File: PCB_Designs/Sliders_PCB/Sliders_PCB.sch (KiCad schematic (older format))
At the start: 7 parts, among them P1 CONN_01X06

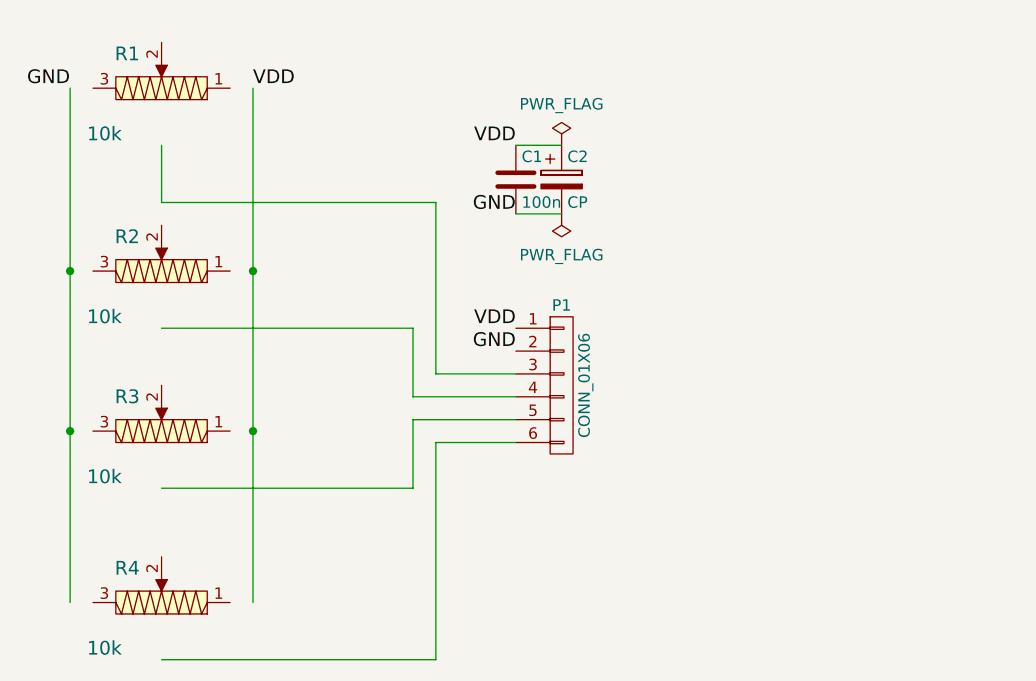
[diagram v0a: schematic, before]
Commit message: PTA6043, Sliders_PCB
Added:
PTA 6043 .lib and .pretty

Drew traces to Sliders_PCB (v1)
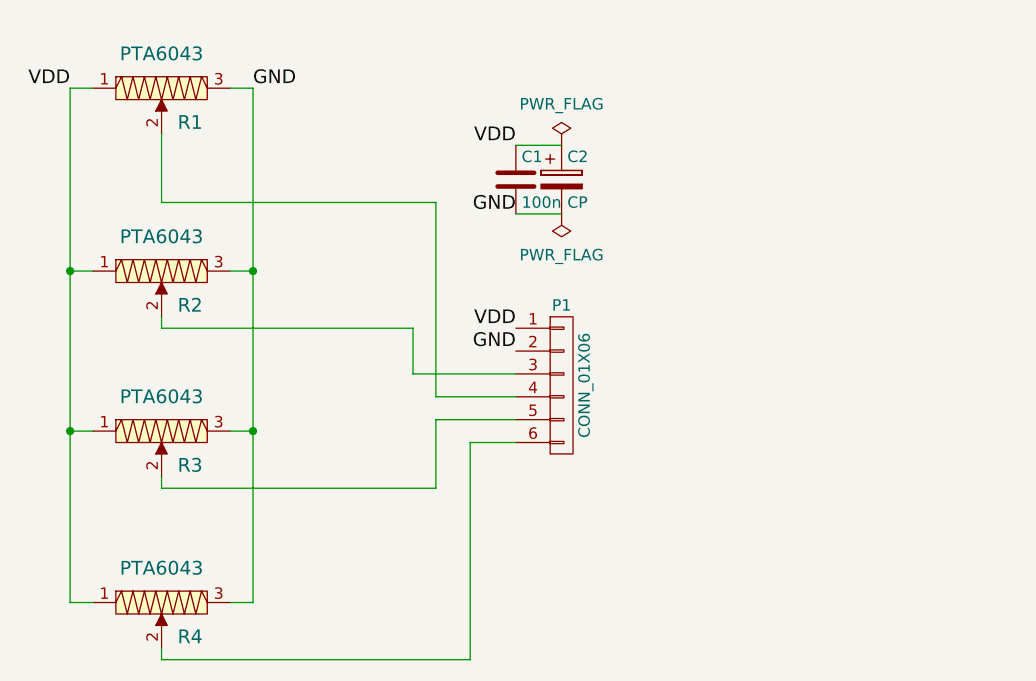
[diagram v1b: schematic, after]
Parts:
- R1, R2, R3, R4: value 10k -> PTA6043; footprint PTA6043:PTA6043 -> Potentiometers_Bourne:Potentiometer_Bourns-PTA6043
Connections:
- wire segments 17 -> 28
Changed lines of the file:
@@
 EESchema Schematic File Version 2
-LIBS:PTA6043
+LIBS:Custom_Switches
 LIBS:mcdts2-4n
-LIBS:conn_01x06_Buttons
 LIBS:power
 LIBS:device
@@
 LIBS:contrib
 LIBS:valves
+LIBS:Slide_Potentiometer
 LIBS:Sliders_PCB-cache
 EELAYER 25 0
@@
 $EndDescr
 $Comp
-L PTA6043 R4
-U 1 1 588B4999
-P 4650 3250
-F 0 "R4" H 4800 3100 60  0000 C CNN
-F 1 "10k" H 4900 3450 60  0000 C CNN
-F 2 "PTA6043:PTA6043" H 4650 3250 60  0001 C CNN
-F 3 "" H 4650 3250 60  0001 C CNN
-	1    4650 3250
-	-1   0    0    1
-$EndComp
-$Comp
-L PTA6043 R3
-U 1 1 588B4A8C
-P 4650 2500
-F 0 "R3" H 4800 2350 60  0000 C CNN
-F 1 "10k" H 4900 2700 60  0000 C CNN
-F 2 "PTA6043:PTA6043" H 4650 2500 60  0001 C CNN
-F 3 "" H 4650 2500 60  0001 C CNN
-	1    4650 2500
-	-1   0    0    1
-$EndComp
-$Comp
-L PTA6043 R2
-U 1 1 588B4AAC
-P 4650 1800
-F 0 "R2" H 4800 1650 60  0000 C CNN
-F 1 "10k" H 4900 2000 60  0000 C CNN
-F 2 "PTA6043:PTA6043" H 4650 1800 60  0001 C CNN
-F 3 "" H 4650 1800 60  0001 C CNN
-	1    4650 1800
-	-1   0    0    1
-$EndComp
-$Comp
-L PTA6043 R1
-U 1 1 588B4B8B
-P 4650 1000
-F 0 "R1" H 4800 850 60  0000 C CNN
-F 1 "10k" H 4900 1200 60  0000 C CNN
-F 2 "PTA6043:PTA6043" H 4650 1000 60  0001 C CNN
-F 3 "" H 4650 1000 60  0001 C CNN
-	1    4650 1000
-	-1   0    0    1
-$EndComp
-$Comp
 L CONN_01X06 P1
 U 1 1 588B4D25
@@
 	1    0    0    -1
 $EndComp
+Text Label 4250 1000 2    60   ~ 0
+VDD
 Text Label 5050 1000 0    60   ~ 0
-VDD
-Text Label 4250 1000 2    60   ~ 0
 GND
 Wire Wire Line
@@
 Connection ~ 4250 2500
 Wire Wire Line
-	4650 1250 4650 1500
+	4650 1200 4650 1500
 Wire Wire Line
 	4650 1500 5850 1500
 Wire Wire Line
-	5850 1500 5850 2250
-Wire Wire Line
-	5850 2250 6200 2250
-Wire Wire Line
-	6200 2350 5750 2350
-Wire Wire Line
-	5750 2350 5750 2050
+	5850 1500 5850 2350
 Wire Wire Line
 	5750 2050 4650 2050
 Wire Wire Line
-	4650 2750 5750 2750
-Wire Wire Line
-	5750 2750 5750 2450
-Wire Wire Line
-	5750 2450 6200 2450
-Wire Wire Line
-	6200 2550 5850 2550
-Wire Wire Line
-	5850 2550 5850 3500
-Wire Wire Line
-	5850 3500 4650 3500
+	4650 3500 6000 3500
 $Comp
 L PWR_FLAG #GND02
@@
 	1    0    0    -1
 $EndComp
+$Comp
+L PTA6043 R1
+U 1 1 589238E9
+P 4650 1000
+F 0 "R1" H 4775 850 60  0000 C CNN
+F 1 "PTA6043" H 4650 1150 60  0000 C CNN
+F 2 "Potentiometers_Bourne:Potentiometer_Bourns-PTA6043" H 4600 1375 60  0001 C CNN
+F 3 "" H 4600 1375 60  0001 C CNN
+	1    4650 1000
+	1    0    0    -1
+$EndComp
+Wire Wire Line
+	4250 1000 4350 1000
+Wire Wire Line
+	4950 1000 5050 1000
+$Comp
+L PTA6043 R2
+U 1 1 589239B0
+P 4650 1800
+F 0 "R2" H 4775 1650 60  0000 C CNN
+F 1 "PTA6043" H 4650 1950 60  0000 C CNN
+F 2 "Potentiometers_Bourne:Potentiometer_Bourns-PTA6043" H 4600 2175 60  0001 C CNN
+F 3 "" H 4600 2175 60  0001 C CNN
+	1    4650 1800
+	1    0    0    -1
+$EndComp
+$Comp
+L PTA6043 R4
+U 1 1 589239FB
+P 4650 3250
+F 0 "R4" H 4775 3100 60  0000 C CNN
+F 1 "PTA6043" H 4650 3400 60  0000 C CNN
+F 2 "Potentiometers_Bourne:Potentiometer_Bourns-PTA6043" H 4600 3625 60  0001 C CNN
+F 3 "" H 4600 3625 60  0001 C CNN
+	1    4650 3250
+	1    0    0    -1
+$EndComp
+$Comp
+L PTA6043 R3
+U 1 1 58923A9D
+P 4650 2500
+F 0 "R3" H 4775 2350 60  0000 C CNN
+F 1 "PTA6043" H 4650 2650 60  0000 C CNN
+F 2 "Potentiometers_Bourne:Potentiometer_Bourns-PTA6043" H 4600 2875 60  0001 C CNN
+F 3 "" H 4600 2875 60  0001 C CNN
+	1    4650 2500
+	1    0    0    -1
+$EndComp
+Wire Wire Line
+	4250 1800 4350 1800
+Wire Wire Line
+	4650 2050 4650 2000
+Wire Wire Line
+	4950 1800 5050 1800
+Wire Wire Line
+	4650 2700 4650 2750
+Wire Wire Line
+	4250 2500 4350 2500
+Wire Wire Line
+	4950 2500 5050 2500
+Wire Wire Line
+	4250 3250 4350 3250
+Wire Wire Line
+	4650 3500 4650 3450
+Wire Wire Line
+	5050 3250 4950 3250
+Wire Wire Line
+	5850 2350 6200 2350
+Wire Wire Line
+	5750 2050 5750 2250
+Wire Wire Line
+	5750 2250 6200 2250
+Wire Wire Line
+	4650 2750 5850 2750
+Wire Wire Line
+	5850 2750 5850 2450
+Wire Wire Line
+	5850 2450 6200 2450
+Wire Wire Line
+	6000 3500 6000 2550
+Wire Wire Line
+	6000 2550 6200 2550
 $EndSCHEMATC

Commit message: Sliders v2
Sliders_PCB klara
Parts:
- removed C2: CP, Capacitors_SMD:CP_Elec_4x4.5, symbol CP
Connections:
- net at P1.3 (P3): now also R1.2; no longer R2.2
- net at P1.4 (P4): now also R2.2; no longer R1.2
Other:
- moved on the sheet: C1
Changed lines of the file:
@@
 Text Label 6200 2150 2    60   ~ 0
 GND
-Text Label 6200 1250 2    60   ~ 0
+Text Label 6450 1250 2    60   ~ 0
 VDD
 $Comp
 L C C1
 U 1 1 588B503E
-P 6200 1400
-F 0 "C1" H 6225 1500 50  0000 L CNN
-F 1 "100n" H 6225 1300 50  0000 L CNN
-F 2 "Capacitors_SMD:C_0603_HandSoldering" H 6238 1250 50  0001 C CNN
-F 3 "" H 6200 1400 50  0000 C CNN
-	1    6200 1400
+P 6650 1400
+F 0 "C1" H 6675 1500 50  0000 L CNN
+F 1 "100n" H 6675 1300 50  0000 L CNN
+F 2 "Capacitors_SMD:C_0603_HandSoldering" H 6688 1250 50  0001 C CNN
+F 3 "" H 6650 1400 50  0000 C CNN
+	1    6650 1400
 	1    0    0    -1
 $EndComp
-Text Label 6200 1550 2    60   ~ 0
+Text Label 6450 1550 2    60   ~ 0
 GND
 $Comp
 L PWR_FLAG #VDD01
 U 1 1 588B50BE
-P 6400 1250
-F 0 "#VDD01" H 6400 1345 50  0001 C CNN
-F 1 "PWR_FLAG" H 6400 1430 50  0000 C CNN
-F 2 "" H 6400 1250 50  0000 C CNN
-F 3 "" H 6400 1250 50  0000 C CNN
-	1    6400 1250
+P 6650 1250
+F 0 "#VDD01" H 6650 1345 50  0001 C CNN
+F 1 "PWR_FLAG" H 6650 1430 50  0000 C CNN
+F 2 "" H 6650 1250 50  0000 C CNN
+F 3 "" H 6650 1250 50  0000 C CNN
+	1    6650 1250
 	1    0    0    -1
 $EndComp
@@
 GND
 Wire Wire Line
-	6200 1550 6400 1550
+	6450 1550 6650 1550
 Wire Wire Line
-	6400 1250 6200 1250
+	6650 1250 6450 1250
 Wire Wire Line
 	5050 1000 5050 3250
@@
 	4650 1200 4650 1500
 Wire Wire Line
-	4650 1500 5850 1500
+	4650 1500 6000 1500
 Wire Wire Line
-	5850 1500 5850 2350
+	6000 1500 6000 2250
 Wire Wire Line
-	5750 2050 4650 2050
+	5850 2050 4650 2050
 Wire Wire Line
 	4650 3500 6000 3500
@@
 L PWR_FLAG #GND02
 U 1 1 588B6CB3
-P 6400 1550
-F 0 "#GND02" H 6400 1645 50  0001 C CNN
-F 1 "PWR_FLAG" H 6400 1730 50  0000 C CNN
-F 2 "" H 6400 1550 50  0000 C CNN
-F 3 "" H 6400 1550 50  0000 C CNN
-	1    6400 1550
+P 6650 1550
+F 0 "#GND02" H 6650 1645 50  0001 C CNN
+F 1 "PWR_FLAG" H 6650 1730 50  0000 C CNN
+F 2 "" H 6650 1550 50  0000 C CNN
+F 3 "" H 6650 1550 50  0000 C CNN
+	1    6650 1550
 	-1   0    0    1
-$EndComp
-$Comp
-L CP C2
-U 1 1 588B6F6B
-P 6400 1400
-F 0 "C2" H 6425 1500 50  0000 L CNN
-F 1 "CP" H 6425 1300 50  0000 L CNN
-F 2 "Capacitors_SMD:CP_Elec_4x4.5" H 6438 1250 50  0001 C CNN
-F 3 "" H 6400 1400 50  0000 C CNN
-	1    6400 1400
-	1    0    0    -1
 $EndComp
 $Comp
@@
 	5050 3250 4950 3250
 Wire Wire Line
-	5850 2350 6200 2350
-Wire Wire Line
-	5750 2050 5750 2250
-Wire Wire Line
-	5750 2250 6200 2250
+	5850 2050 5850 2350
 Wire Wire Line
 	4650 2750 5850 2750
@@
 Wire Wire Line
 	6000 2550 6200 2550
+Wire Wire Line
+	6000 2250 6200 2250
+Wire Wire Line
+	5850 2350 6200 2350
 $EndSCHEMATC

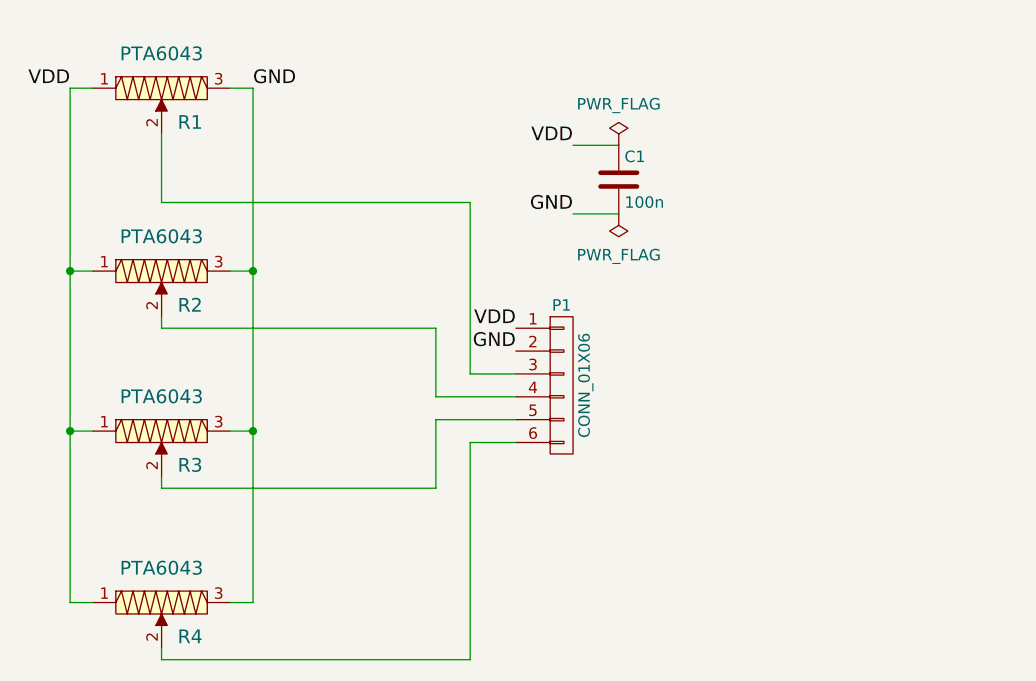
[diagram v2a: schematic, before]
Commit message: Completed all Circuits for evaluation
* All board-to-board connectors now Multicomp 02X05
* Mounting holes for all PCB
* Vias at all groundpins
* Minor other changes
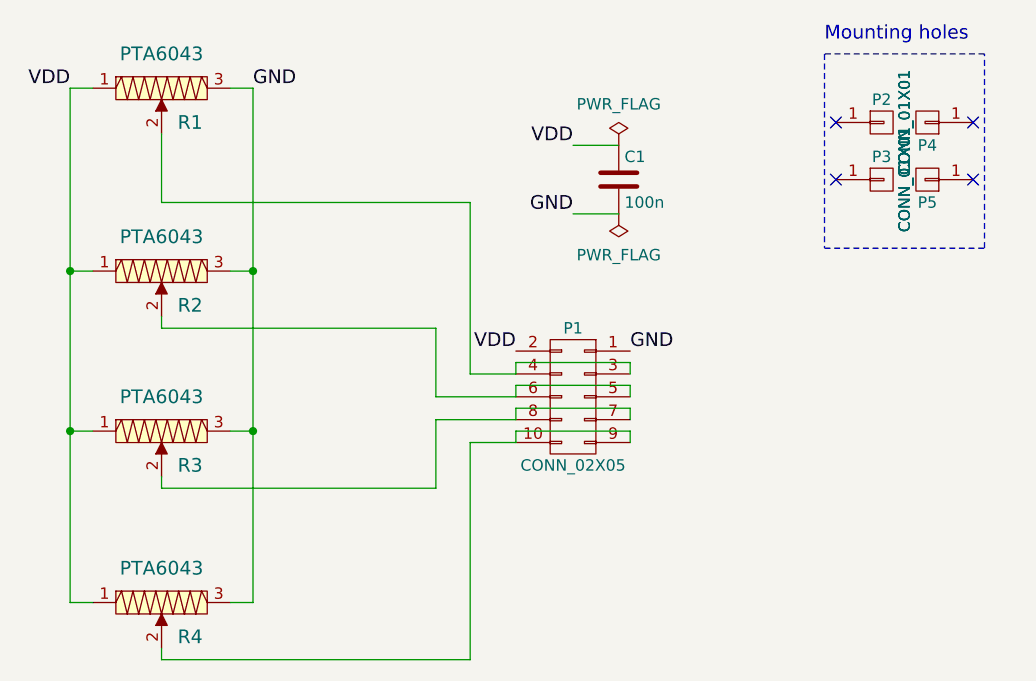
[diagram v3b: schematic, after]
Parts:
- removed P1: CONN_01X06, Socket_Strips:Socket_Strip_Straight_1x06, symbol CONN_01X06
- added P1: CONN_02X05, Connectors_Multicomp:Multicomp_MC9A22-1034_2x05x2.54mm_Angled, symbol CONN_02X05
- added P2, P3, P4, P5: CONN_01X01, Mounting_Holes:MountingHole_2.2mm_M2_DIN965_Pad, symbol CONN_01X01
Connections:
- net GND: now also P1.1 (P1)
- net VDD: now also P1.2 (P2)
- net at R1.2: now also P1.3 (P3), P1.4 (P4)
- net at R2.2: now also P1.5 (P5), P1.6 (P6)
- net at R3.2: now also P1.7 (P7), P1.8 (P8)
- net at R4.2: now also P1.10 (P10), P1.9 (P9)
- no-connect marks 0 -> 4
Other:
- note added: "Mounting holes"
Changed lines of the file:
@@
 Comment4 ""
 $EndDescr
-$Comp
-L CONN_01X06 P1
-U 1 1 588B4D25
-P 6400 2300
-F 0 "P1" H 6400 2650 50  0000 C CNN
-F 1 "CONN_01X06" V 6500 2300 50  0000 C CNN
-F 2 "Socket_Strips:Socket_Strip_Straight_1x06" H 6400 2300 50  0001 C CNN
-F 3 "" H 6400 2300 50  0000 C CNN
-	1    6400 2300
-	1    0    0    -1
-$EndComp
-Text Label 6200 2050 2    60   ~ 0
+Text Label 6200 2150 2    60   ~ 0
 VDD
-Text Label 6200 2150 2    60   ~ 0
+Text Label 6700 2150 0    60   ~ 0
 GND
 Text Label 6450 1250 2    60   ~ 0
@@
 Wire Wire Line
 	5850 2350 6200 2350
+$Comp
+L CONN_02X05 P1
+U 1 1 58A664D3
+P 6450 2350
+F 0 "P1" H 6450 2650 50  0000 C CNN
+F 1 "CONN_02X05" H 6450 2050 50  0000 C CNN
+F 2 "Connectors_Multicomp:Multicomp_MC9A22-1034_2x05x2.54mm_Angled" H 6450 1150 50  0001 C CNN
+F 3 "" H 6450 1150 50  0001 C CNN
+	1    6450 2350
+	-1   0    0    -1
+$EndComp
+Wire Wire Line
+	6200 2250 6200 2200
+Wire Wire Line
+	6200 2200 6700 2200
+Wire Wire Line
+	6700 2200 6700 2250
+Wire Wire Line
+	6200 2350 6200 2300
+Wire Wire Line
+	6200 2300 6700 2300
+Wire Wire Line
+	6700 2300 6700 2350
+Wire Wire Line
+	6700 2450 6700 2400
+Wire Wire Line
+	6700 2400 6200 2400
+Wire Wire Line
+	6200 2400 6200 2450
+Wire Wire Line
+	6200 2550 6200 2500
+Wire Wire Line
+	6200 2500 6700 2500
+Wire Wire Line
+	6700 2500 6700 2550
+$Comp
+L CONN_01X01 P2
+U 1 1 58A619C7
+P 7800 1150
+F 0 "P2" H 7800 1250 50  0000 C CNN
+F 1 "CONN_01X01" V 7900 1150 50  0000 C CNN
+F 2 "Mounting_Holes:MountingHole_2.2mm_M2_DIN965_Pad" H 7800 1150 50  0001 C CNN
+F 3 "" H 7800 1150 50  0001 C CNN
+	1    7800 1150
+	1    0    0    -1
+$EndComp
+$Comp
+L CONN_01X01 P3
+U 1 1 58A61A91
+P 7800 1400
+F 0 "P3" H 7800 1500 50  0000 C CNN
+F 1 "CONN_01X01" V 7900 1400 50  0000 C CNN
+F 2 "Mounting_Holes:MountingHole_2.2mm_M2_DIN965_Pad" H 7800 1400 50  0001 C CNN
+F 3 "" H 7800 1400 50  0001 C CNN
+	1    7800 1400
+	1    0    0    -1
+$EndComp
+$Comp
+L CONN_01X01 P4
+U 1 1 58A61AF0
+P 8000 1150
+F 0 "P4" H 8000 1250 50  0000 C CNN
+F 1 "CONN_01X01" V 8100 1150 50  0000 C CNN
+F 2 "Mounting_Holes:MountingHole_2.2mm_M2_DIN965_Pad" H 8000 1150 50  0001 C CNN
+F 3 "" H 8000 1150 50  0001 C CNN
+	1    8000 1150
+	-1   0    0    1
+$EndComp
+$Comp
+L CONN_01X01 P5
+U 1 1 58A61B35
+P 8000 1400
+F 0 "P5" H 8000 1500 50  0000 C CNN
+F 1 "CONN_01X01" V 8100 1400 50  0000 C CNN
+F 2 "Mounting_Holes:MountingHole_2.2mm_M2_DIN965_Pad" H 8000 1400 50  0001 C CNN
+F 3 "" H 8000 1400 50  0001 C CNN
+	1    8000 1400
+	-1   0    0    1
+$EndComp
+Wire Notes Line
+	8250 850  7550 850
+Wire Notes Line
+	7550 850  7550 1700
+Wire Notes Line
+	7550 1700 8250 1700
+Wire Notes Line
+	8250 1700 8250 850
+Text Notes 7550 800  0    60   ~ 0
+Mounting holes
+NoConn ~ 7600 1150
+NoConn ~ 7600 1400
+NoConn ~ 8200 1150
+NoConn ~ 8200 1400
 $EndSCHEMATC
